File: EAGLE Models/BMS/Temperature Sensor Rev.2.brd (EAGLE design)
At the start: 160 x 100 mm, 5 parts, among them IC2 TL331

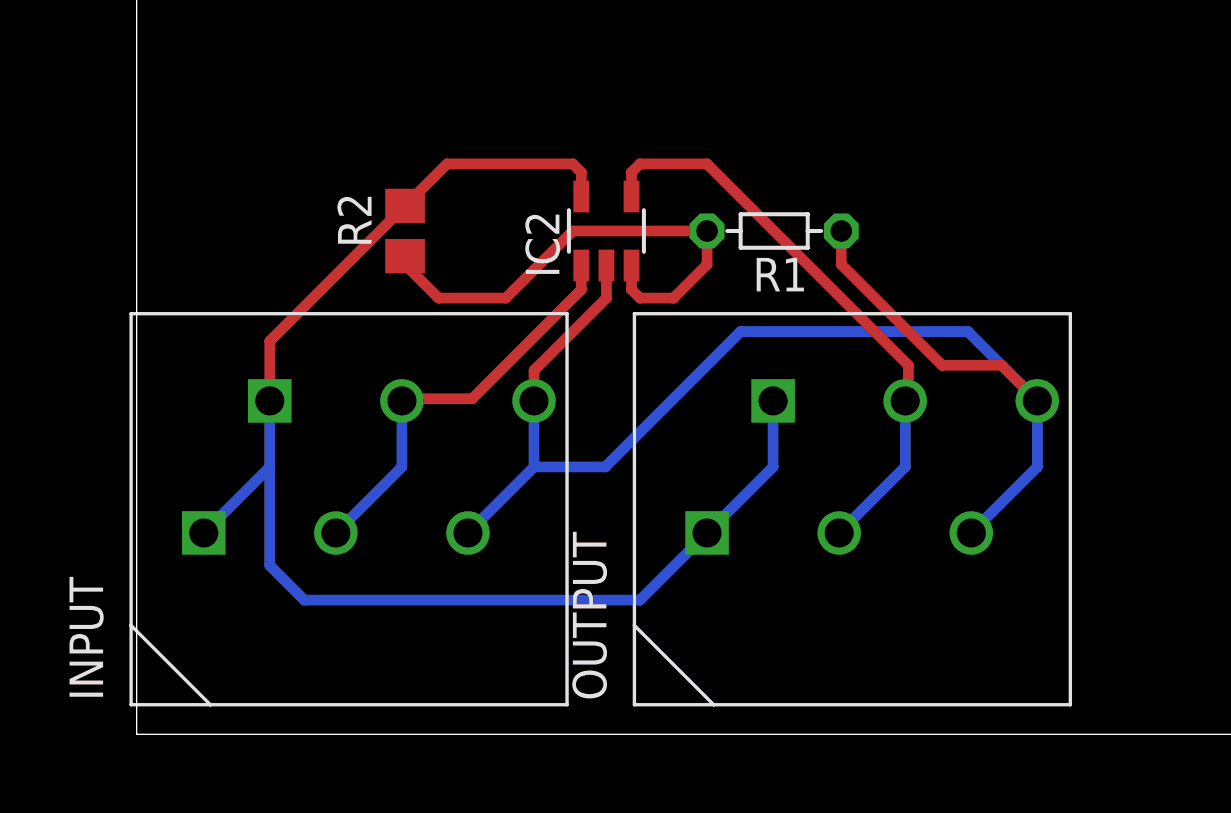
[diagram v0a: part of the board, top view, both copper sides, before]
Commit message: Added second option for temperature sensor
Switched to soldered wires instead of connectors to reduce size. May not
be necessary if new connection method is developed.
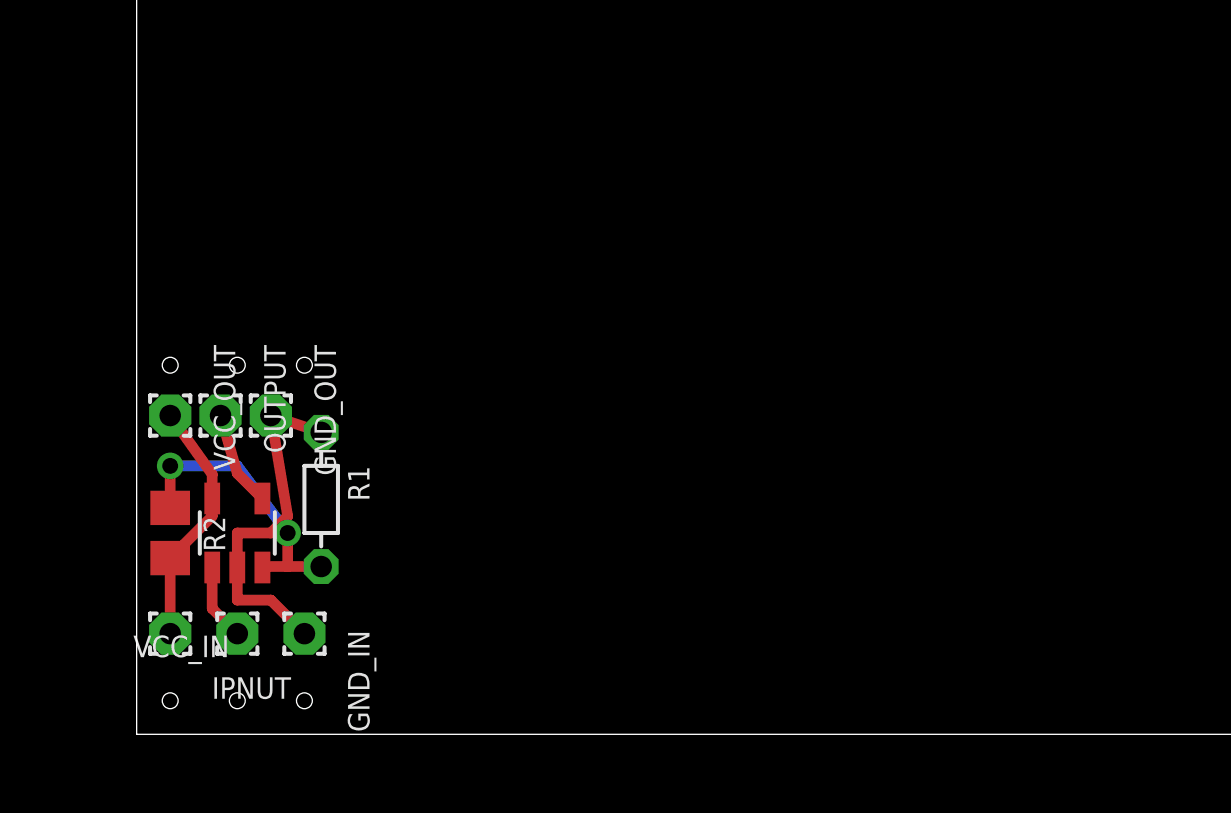
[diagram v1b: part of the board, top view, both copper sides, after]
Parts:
- removed INPUT: CONN_3, formula electric:CONNECTOR_3
- added GND_IN, GND_OUT, IPNUT, VCC_IN, VCC_OUT: (no value), wirepad:1,6/0,8
- OUTPUT: value CONN_3 -> (none); device formula electric:CONNECTOR_3 -> wirepad:1,6/0,8
- moved R1 19.9 mm to (6.99, 8.89), turned to 270 degrees
- moved OUTPUT 18.9 mm to (3.17, 12.1), turned to 180 degrees
- moved IC2 18.1 mm to (3.81, 7.62)
- moved R2 14.5 mm to (1.27, 7.62), turned to 270 degrees
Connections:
- net GND: now also GND_IN.1, GND_OUT.1; no longer INPUT.5, INPUT.6, OUTPUT.5, OUTPUT.6
- net INPUT: now also IPNUT.1; no longer INPUT.3, INPUT.4
- net OUTPUT: now also OUTPUT.1; no longer OUTPUT.3, OUTPUT.4
- net VCC: now also VCC_IN.1, VCC_OUT.1; no longer INPUT.1, INPUT.2, OUTPUT.1, OUTPUT.2
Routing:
- net VCC: track 51.8 -> 9.42 mm
- net GND: track 51.4 -> 13.6 mm
- net OUTPUT: track 22.1 -> 3.62 mm
- net INPUT: track 15.5 -> 2.90 mm
- net N$1: track 19.0 -> 10.8 mm, vias 0 -> 2

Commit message: Made an okboard layout
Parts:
- added R3, R4: (no value), resistor:R0603
- added T$1: THERMISTOR, formula electric:0603
- added _: DMG6602, formula electric:SOT23-6
- R1: value THERMISTOR-5 -> (none); device varistor:R-5 -> resistor:R0603
- R2: device resistor:R0805 -> resistor:R0603
- moved IPNUT 14.6 mm to (12.1, 15.9), turned to 0 degrees
- moved VCC_IN 13.6 mm to (7.62, 15.9), turned to 0 degrees
- moved GND_IN 12.7 mm to (2.54, 15.9)
- moved OUTPUT 12.6 mm to (12.7, 3.81), turned to 0 degrees
- moved VCC_OUT 10.4 mm to (7.62, 3.81)
- moved GND_OUT 8.64 mm to (2.54, 3.81)
- moved R1 5.12 mm to (11.4, 11.4)
- moved R2 4.96 mm to (4.45, 11.4), flipped to the bottom, turned to 90 degrees
- moved IC2 3.81 mm to (7.62, 7.62), flipped to the bottom, turned to 90 degrees
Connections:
- removed net N$1: IC2.3, R1.2, R2.1
- new net COMP_OUT: IC2.4, R1.2, R3.2
- new net MOS_IN: R1.1, _.P$1, _.P$3
- new net THERM_OUT: IC2.3, R2.2, T$1.P$1, _.P$4
- net GND: now also R4.2, T$1.P$2; no longer R1.1
- net INPUT: now also R4.1, _.P$6
- net OUTPUT: now also _.P$2, _.P$5; no longer IC2.4
- net VCC: now also R2.1, R3.1; no longer R2.2
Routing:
- net INPUT: track 2.90 -> 43.9 mm
- net THERM_OUT: track 0.00 -> 16.1 mm, vias 0 -> 1
- net VCC: track 9.42 -> 24.8 mm
- net GND: track 13.6 -> 0.00 mm
- net N$1: track 10.8 -> 0.00 mm, vias 2 -> 0
- net OUTPUT: track 3.62 -> 13.3 mm
- net MOS_IN: track 0.00 -> 9.47 mm
- net COMP_OUT: track 0.00 -> 7.83 mm, vias 0 -> 1
- added copper zone on layer 1, net GND
- added copper zone on layer 16, net GND
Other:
- board size 160 x 100 mm -> 16.7 x 22 mm
